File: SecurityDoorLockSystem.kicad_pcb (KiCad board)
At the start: 2 copper layers, 86 x 56 mm, 12 parts, among them J1 Power In, J2 Servo, J3 RFID-RC522, J4 R307s, U1 ESP32-DEVKIT-V1, U2 L7805

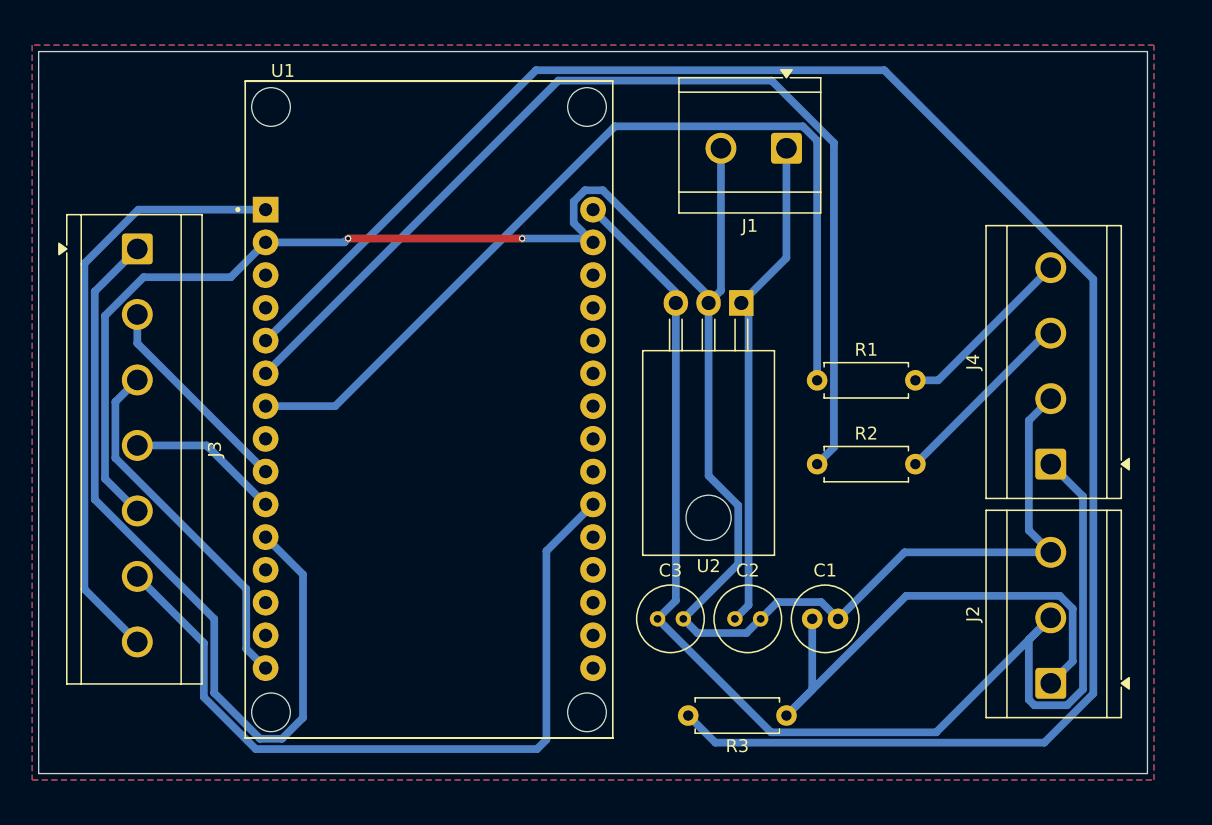
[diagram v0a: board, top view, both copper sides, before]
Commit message: added: protection -- modified: pcb, schematic
added power source polarity protection
changed tracks (sizes and routes)
changed schematic diagram connectors to screw terminals
changed pcb connectors to screw terminals
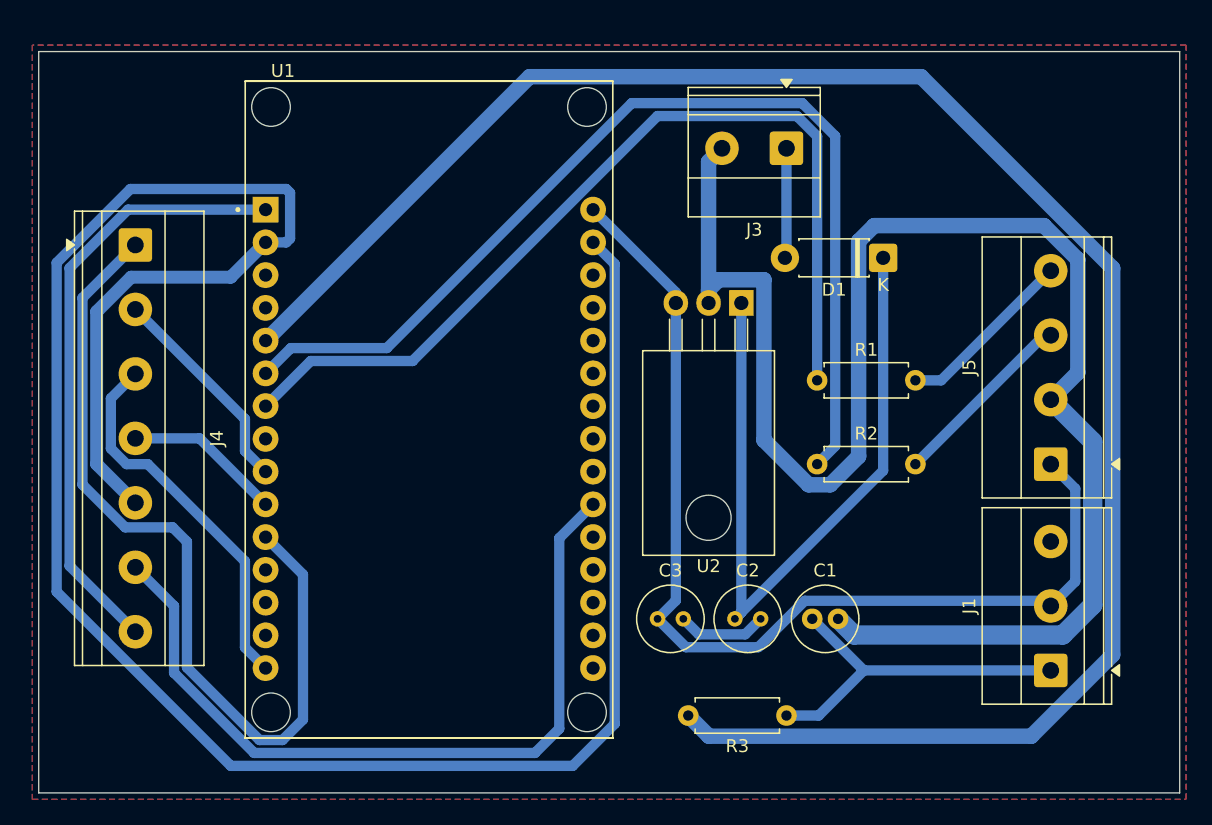
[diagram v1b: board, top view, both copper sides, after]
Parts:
- removed J2: Servo, TerminalBlock_CUI:TerminalBlock_CUI_TB007-508-03_1x03_P5.08mm_Horizontal
- added D1: 1N5817, Diode_THT:D_DO-41_SOD81_P7.62mm_Horizontal, F.Cu at (153.5, 69.0)
- added J5: R307s, TerminalBlock_Phoenix:TerminalBlock_Phoenix_MKDS-1,5-4_1x04_P5.00mm_Horizontal, F.Cu at (166.5, 85.0)
- J1: value Power In -> Servo; footprint TerminalBlock_CUI:TerminalBlock_CUI_TB007-508-02_1x02_P5.08mm_Horizontal -> TerminalBlock_Phoenix:TerminalBlock_Phoenix_MKDS-1,5-3_1x03_P5.00mm_Horizontal
- J3: value RFID-RC522 -> Power In; footprint TerminalBlock_CUI:TerminalBlock_CUI_TB007-508-07_1x07_P5.08mm_Horizontal -> TerminalBlock_Phoenix:TerminalBlock_Phoenix_MKDS-1,5-2_1x02_P5.00mm_Horizontal
- J4: value R307s -> RFID-RC522; footprint TerminalBlock_CUI:TerminalBlock_CUI_TB007-508-04_1x04_P5.08mm_Horizontal -> TerminalBlock_Phoenix:TerminalBlock_Phoenix_MKDS-1,5-7_1x07_P5.00mm_Horizontal
- moved J4 73.0 mm to (95.5, 68.0), turned to -90 degrees
- moved J3 51.0 mm to (146.0, 60.5), turned to 180 degrees
- moved J1 45.4 mm to (166.5, 101.0), turned to 90 degrees
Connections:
- J1 pad 1: /VCC -> /Servo Signal
- J1 pad 2: GND -> /5V
- J3 pad 1: /SDA -> Net-(D1-A)
- J3 pad 2: /SCK -> GND
- J4 pad 1: /5V -> /SDA
- J4 pad 2: GND -> /SCK
- J4 pad 3: /Receiver -> /MOSI
- J4 pad 4: /Transmitter -> /MISO
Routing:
- net GND: track 160.8 -> 304.1 mm, vias 2 -> 0
- net /5V: track 103.3 -> 80.6 mm
- net /VCC: track 38.6 -> 57.5 mm
- net /Servo Signal: track 41.3 -> 27.6 mm
- net Net-(D1-A): track 0.00 -> 8.55 mm
- net /SDA: track 63.9 -> 67.3 mm
- net /MOSI: track 27.9 -> 29.5 mm
- net /RST: track 59.8 -> 61.1 mm
- net Net-(U1-RX2): track 80.9 -> 79.9 mm
- net Net-(U1-D4): track 145.6 -> 146.5 mm
- net Net-(U1-TX2): track 70.8 -> 71.7 mm
- net /3v3: track 46.8 -> 47.4 mm
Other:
- board size 86 x 56 mm -> 88.5 x 57.5 mm

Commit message: modified capacitor values
changed value of capacitors 1 and 2; C1 = 100uF, C2 = 50uF
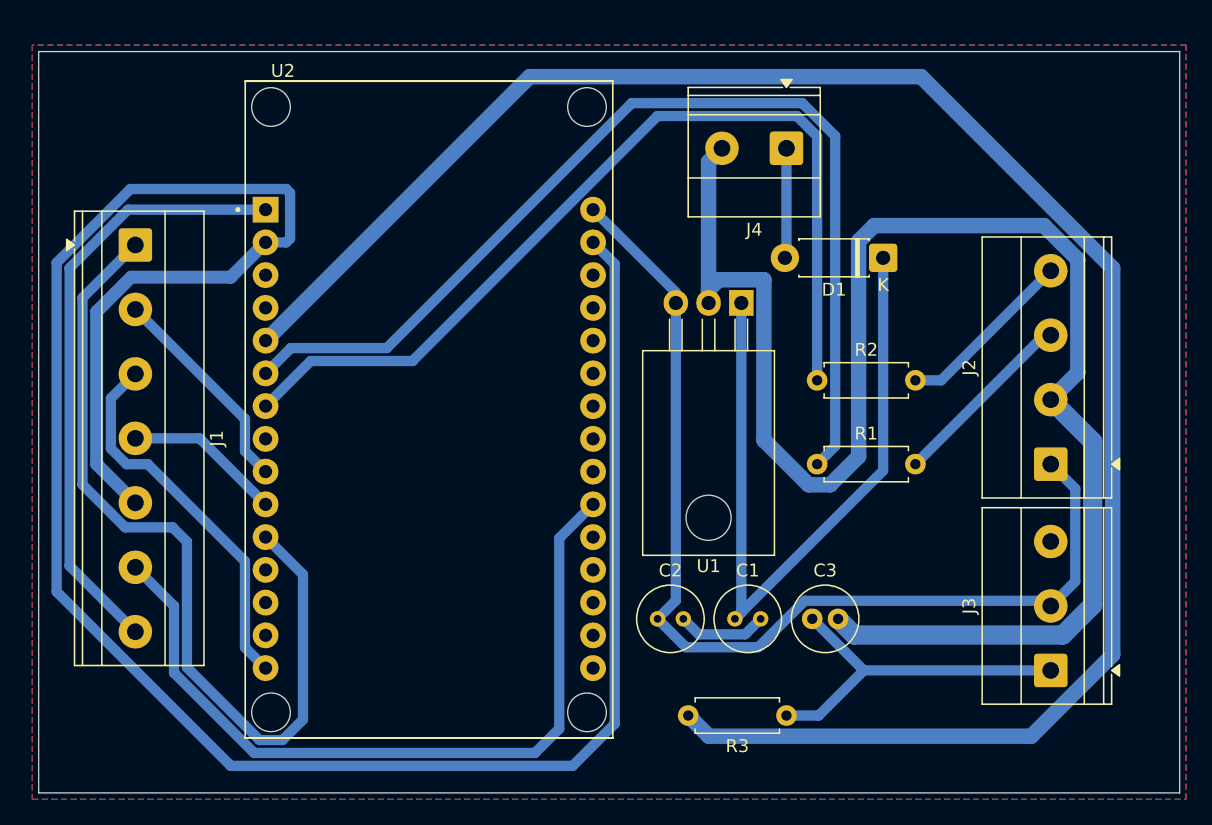
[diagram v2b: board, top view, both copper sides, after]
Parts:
- C1: renamed from C2; value C -> 150uF
- C2: renamed from C3; value C -> 50uF
- renumbered C1 to C3, J4 to J1, J5 to J2, J1 to J3, J3 to J4, R2 to R1, R1 to R2, U2 to U1, U1 to U2

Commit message: modified capacitor values
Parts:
- C1: value 150uF -> 100uF
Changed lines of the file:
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@@
 			)
 		)
-		(property "Value" "150uF"
+		(property "Value" "100uF"
 			(at 1 3.75 0)
 			(layer "F.Fab")

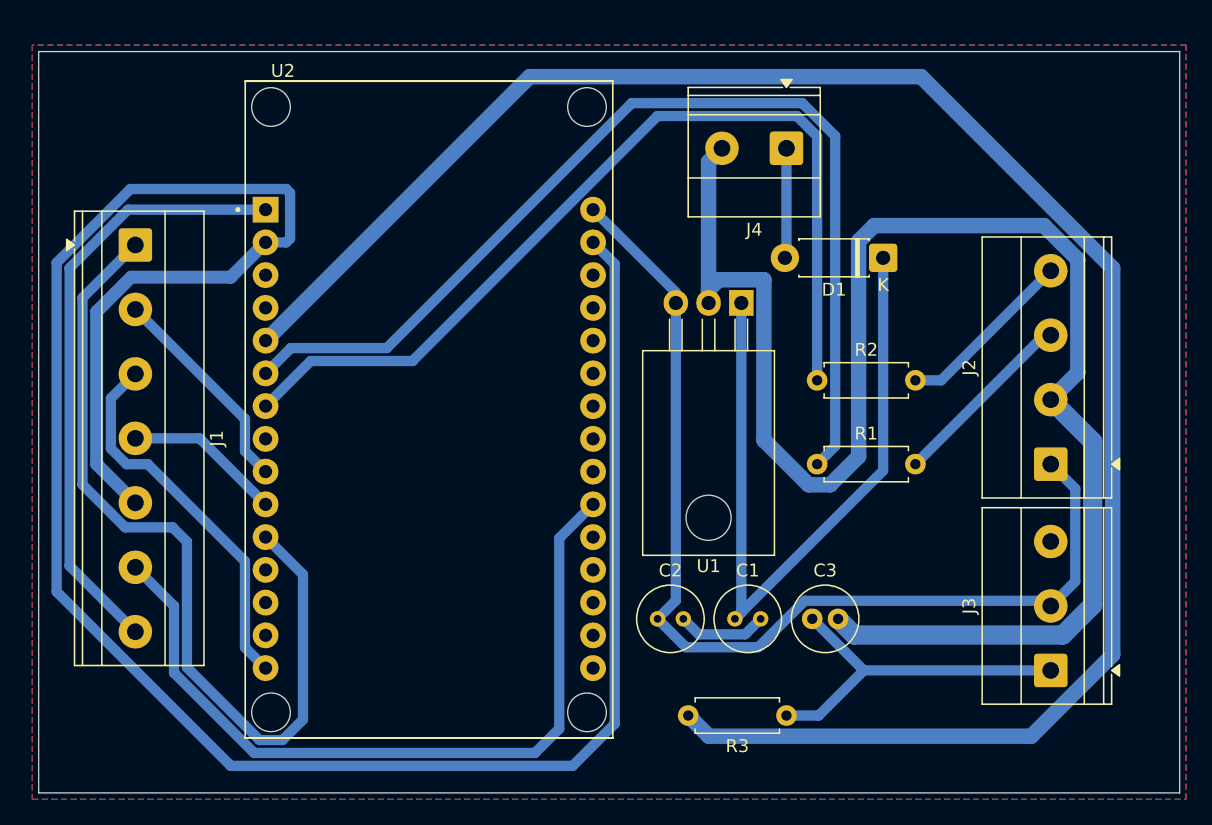
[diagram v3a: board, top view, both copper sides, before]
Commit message: added lcd
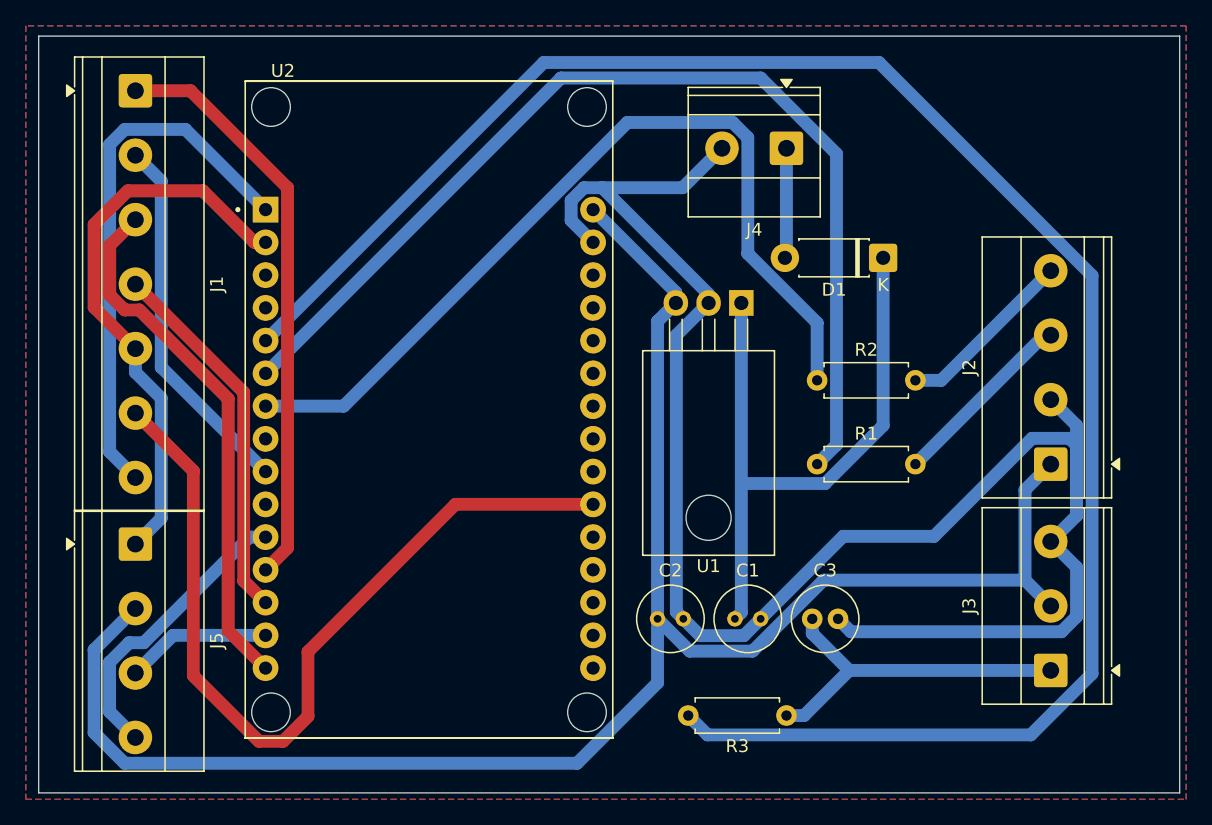
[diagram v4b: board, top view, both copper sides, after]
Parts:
- added J5: LCD Conn, TerminalBlock_Phoenix:TerminalBlock_Phoenix_MKDS-1,5-4_1x04_P5.00mm_Horizontal, F.Cu at (95.5, 91.2)
- C1: value 100uF -> 150uF
- moved J1 12.0 mm to (95.5, 56.0)
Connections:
- J1 pad 1: /SDA -> /Rx
- J1 pad 4: /MISO -> /Tx
- U2 pad 10: /MISO -> unconnected-(U2-D19-Pad10)
- U2 pad 12: unconnected-(U2-RX0-Pad12) -> /Rx
- U2 pad 13: unconnected-(U2-TX0-Pad13) -> /Tx
- U2 pad 14: unconnected-(U2-D22-Pad14) -> /SCL
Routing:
- net GND: track 304.1 -> 181.0 mm
- net /5V: track 80.6 -> 142.6 mm
- net /Rx: track 0.00 -> 45.3 mm
- net /SDA: track 67.3 -> 22.8 mm
- net /Tx: track 0.00 -> 28.9 mm
- net /MISO: track 12.2 -> 0.00 mm
- net /SCK: track 16.8 -> 28.7 mm
- net /MOSI: track 29.5 -> 41.3 mm
- net /SCL: track 0.00 -> 11.3 mm
- net /VCC: track 57.5 -> 50.6 mm
- net /3v3: track 47.4 -> 41.8 mm
- net /RST: track 61.1 -> 65.9 mm
- net Net-(U2-TX2): track 71.7 -> 68.1 mm
- net Net-(U2-D4): track 146.5 -> 144.7 mm
- net Net-(U2-RX2): track 79.9 -> 80.9 mm
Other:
- board size 88.5 x 57.5 mm -> 88.5 x 58.7 mm
